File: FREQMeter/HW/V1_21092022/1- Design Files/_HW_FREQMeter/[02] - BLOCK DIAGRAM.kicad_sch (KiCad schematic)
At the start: 0 parts

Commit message: WORKING ON FREQMeter Hardware
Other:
- note added: "100MHz to 1.1 GHz Ratio 1:16"
- note added: "1Hz to 1MHz Ratio 1:1"
- note added: "1MHz to 100MHz Ratio 1:1024"
- note added: "32 SMD LEDs Binary Counter"
- note added: "4 X SHIFT REGISTER"
- note added: "Data Lines"
- note added: "Page 3"
- note added: "Page 4"
- note added: "Page 5"
- note added: "Page 6"
- note added: "X2 Buffer CLOCK Enable Pin"
- note added: "X2 Data Lines"
- note removed: "100MHz to 1.1 GHz dividing by 16"
- note removed: "1MHz to 100MHz dividing by 1024"
- note removed: "DC (0Hz) to 1MHz Ratio 1:1"

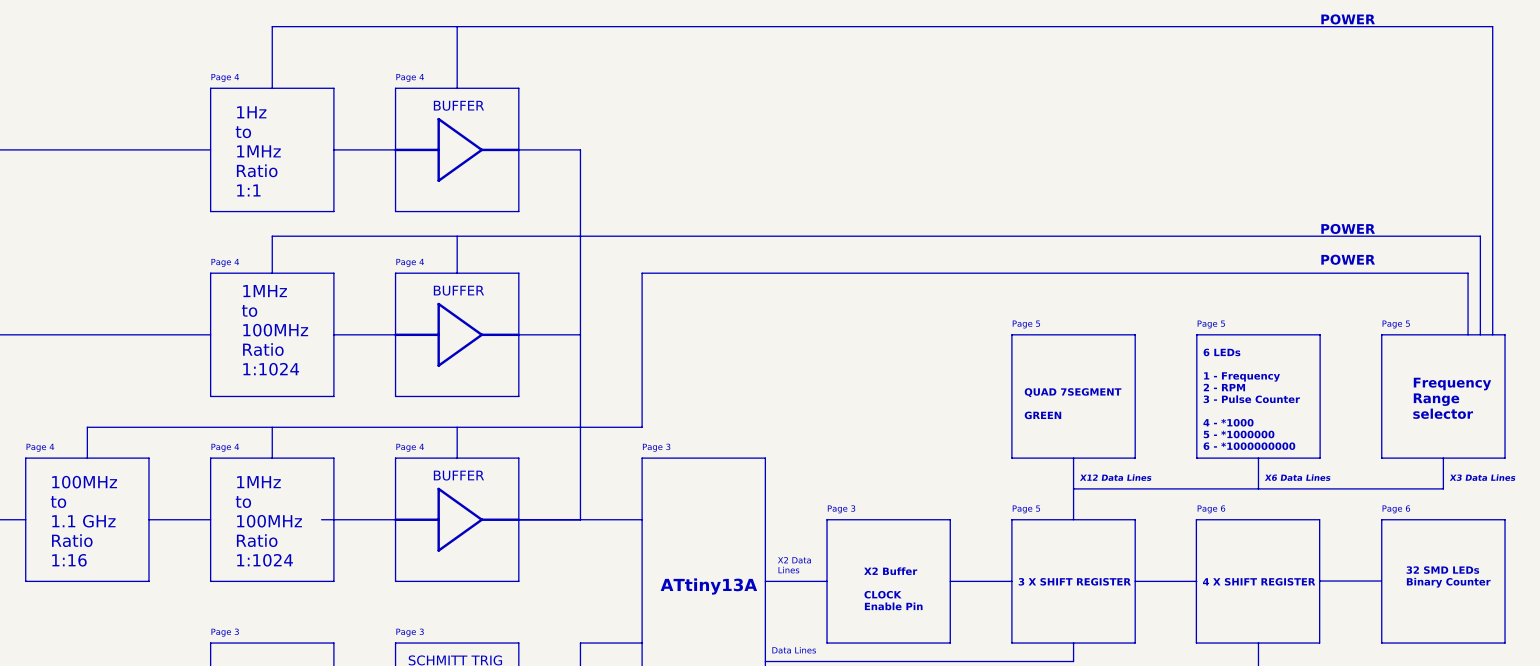
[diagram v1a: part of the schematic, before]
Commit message: progress on Frequency meter hardware
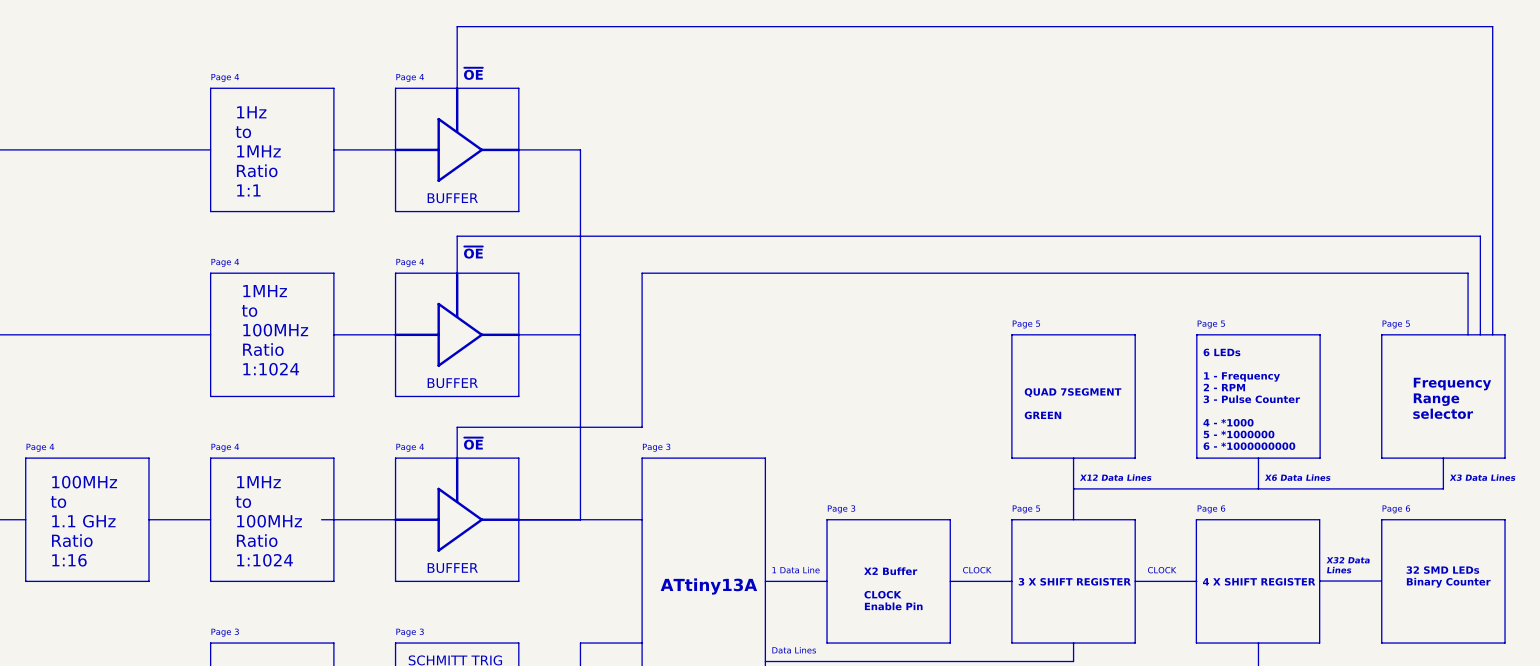
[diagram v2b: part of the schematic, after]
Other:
- note added: "1 Data Line"
- note added: "CLOCK"
- note added: "X32 Data Lines"
- note added: "~{OE}"
- note removed: "POWER"
- note removed: "X2 Data Lines"

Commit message: frequency meter input schematic in progress
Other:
- note added: "BNC Input & Matching Circuit"
- note added: "Filter BPF 1MHz To 99.999MHz"
- note added: "Filter LPF 1Hz To 999KHz"
- note added: "INPUT CIRCUIT"
- note added: "O1"
- note added: "O2"
- note added: "O3"
- note added: "OPEN-LOOP AMPLIFIRE"
- note added: "~{OE1}"
- note added: "~{OE2}"
- note added: "~{OE3}"
- note removed: "1Hz to 1MHz Ratio 1:1"
- note removed: "BNC Input"
- note removed: "Matching Circuit"
- note removed: "~{OE}"

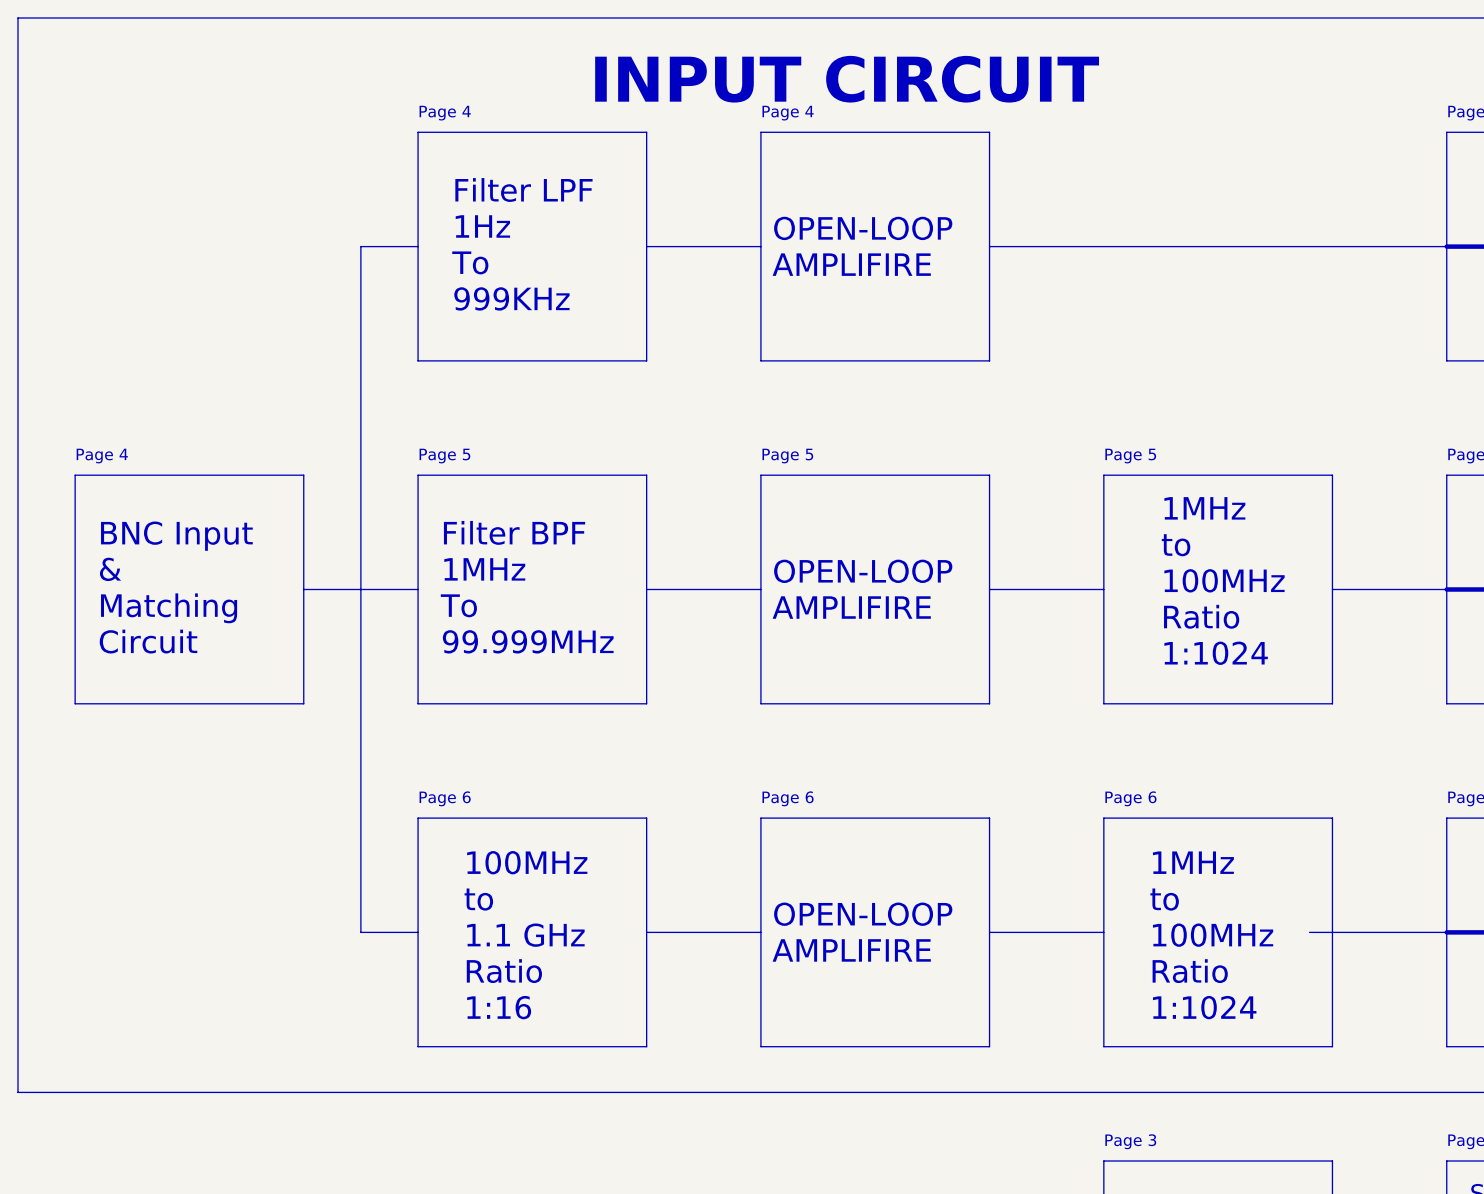
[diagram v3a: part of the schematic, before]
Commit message: Input signal schematic has been modified
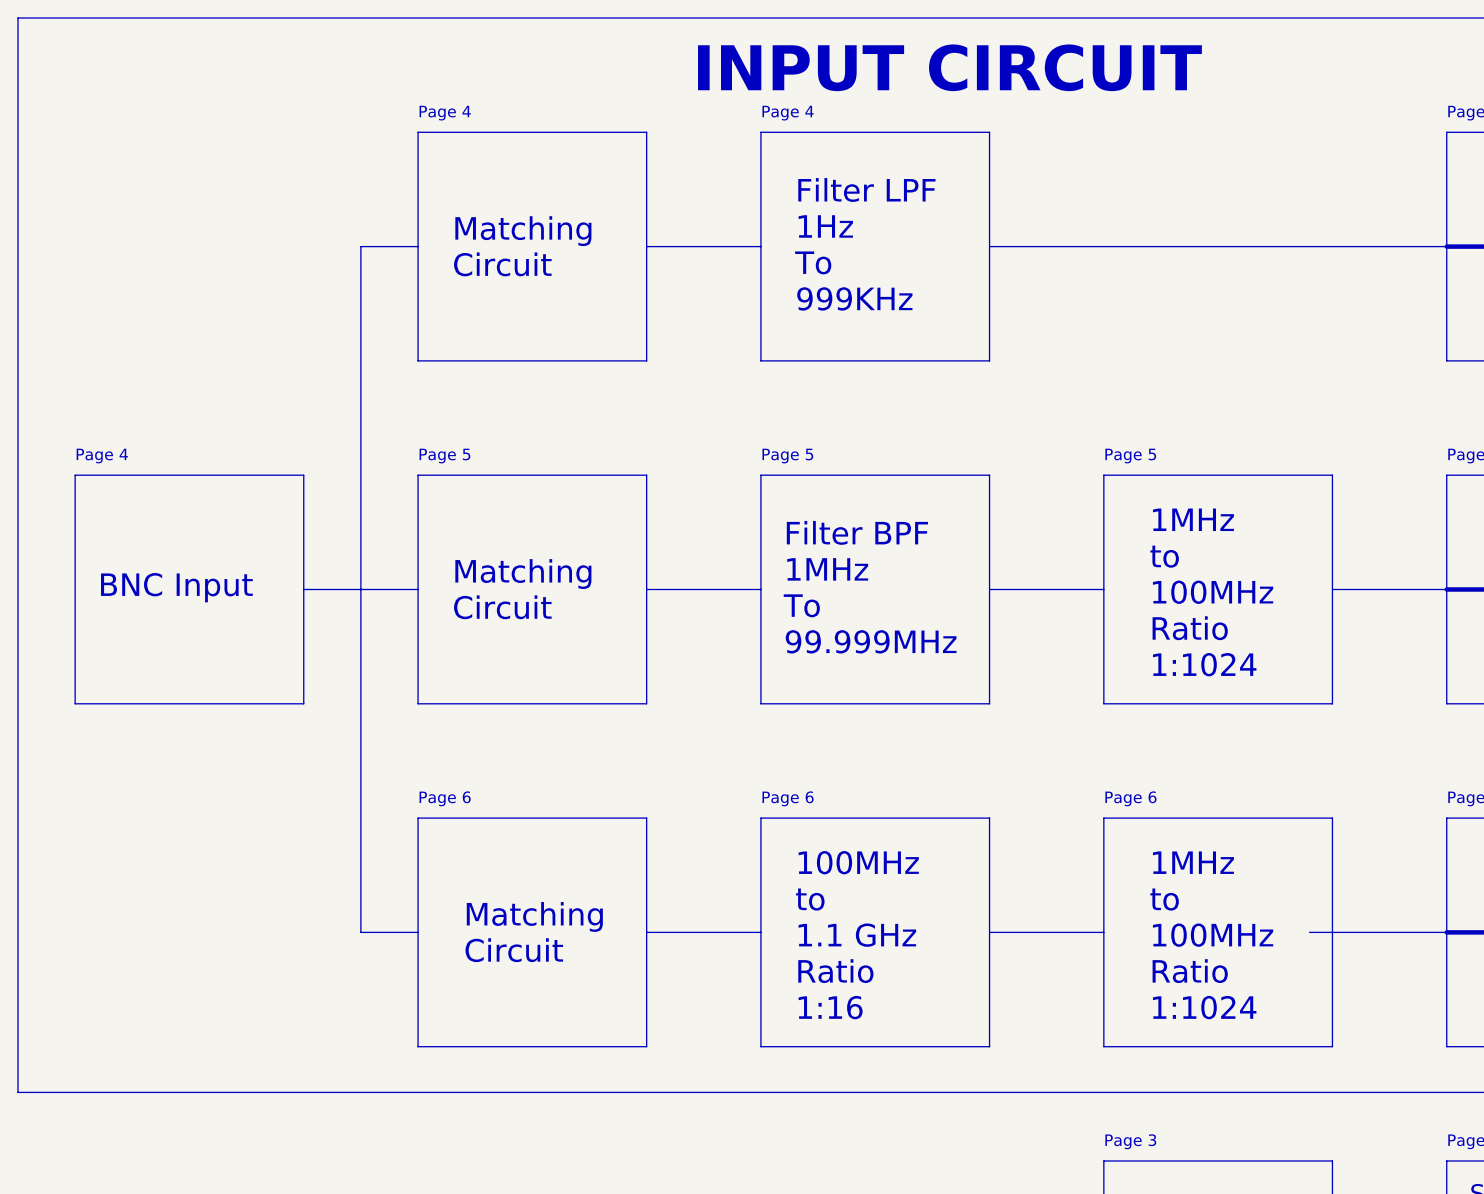
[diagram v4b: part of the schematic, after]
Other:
- note added: "BNC Input"
- note added: "Matching Circuit"
- note removed: "BNC Input & Matching Circuit"
- note removed: "OPEN-LOOP AMPLIFIRE"
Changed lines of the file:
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@@
     (effects (font (size 1.27 1.27)) (justify left bottom))
   )
-  (text "Filter LPF\n1Hz \nTo \n999KHz" (at 67.31 83.82 0)
+  (text "Filter LPF\n1Hz \nTo \n999KHz" (at 105.41 83.82 0)
     (effects (font (size 2.5 2.5)) (justify left bottom))
   )
@@
     (effects (font (size 1.27 1.27)) (justify left bottom))
   )
-  (text "OPEN-LOOP\nAMPLIFIRE" (at 102.87 80.01 0)
-    (effects (font (size 2.5 2.5)) (justify left bottom))
-  )
   (text "X32 Data\nLines" (at 369.57 163.83 0)
     (effects (font (size 1.27 1.27) (thickness 0.254) bold italic) (justify left bottom))
@@
     (effects (font (size 1.27 1.27)) (justify left bottom))
   )
-  (text "Filter BPF\n1MHz\nTo\n99.999MHz" (at 66.04 121.92 0)
+  (text "Filter BPF\n1MHz\nTo\n99.999MHz" (at 104.14 121.92 0)
     (effects (font (size 2.5 2.5)) (justify left bottom))
   )
@@
     (effects (font (size 1.5 1.5) (thickness 0.254) bold) (justify left bottom))
   )
+  (text "Matching \nCircuit" (at 67.31 80.01 0)
+    (effects (font (size 2.5 2.5)) (justify left bottom))
+  )
   (text "Page 5" (at 304.8 113.03 0)
     (effects (font (size 1.27 1.27)) (justify left bottom))
@@
     (effects (font (size 1.27 1.27)) (justify left bottom))
   )
+  (text "Matching \nCircuit" (at 68.58 156.21 0)
+    (effects (font (size 2.5 2.5)) (justify left bottom))
+  )
   (text "3 X SHIFT REGISTER" (at 306.07 166.37 0)
     (effects (font (size 1.5 1.5) (thickness 0.254) bold) (justify left bottom))
+  )
+  (text "Matching \nCircuit" (at 67.31 118.11 0)
+    (effects (font (size 2.5 2.5)) (justify left bottom))
   )
   (text "X6 Data Lines" (at 356.87 144.78 0)
@@
     (effects (font (size 1.5 1.5) (thickness 0.254) bold) (justify left bottom))
   )
-  (text "100MHz\nto\n1.1 GHz \nRatio\n1:16" (at 68.58 162.56 0)
+  (text "100MHz\nto\n1.1 GHz \nRatio\n1:16" (at 105.41 162.56 0)
     (effects (font (size 2.5 2.5)) (justify left bottom))
   )
@@
     (effects (font (size 1.27 1.27) (thickness 0.254) bold italic) (justify left bottom))
   )
-  (text "BNC Input\n&\nMatching \nCircuit" (at 27.94 121.92 0)
+  (text "BNC Input" (at 27.94 115.57 0)
     (effects (font (size 2.5 2.5)) (justify left bottom))
   )
@@
     (effects (font (size 1.27 1.27)) (justify left bottom))
   )
-  (text "1MHz\nto\n100MHz\nRatio\n1:1024" (at 146.05 123.19 0)
+  (text "1MHz\nto\n100MHz\nRatio\n1:1024" (at 144.78 124.46 0)
     (effects (font (size 2.5 2.5)) (justify left bottom))
   )
@@
     (effects (font (size 1.27 1.27)) (justify left bottom))
   )
-  (text "INPUT CIRCUIT" (at 82.55 60.96 0)
+  (text "INPUT CIRCUIT" (at 93.98 59.69 0)
     (effects (font (size 5 5) (thickness 1) bold) (justify left bottom))
   )
@@
     (effects (font (size 1.27 1.27)) (justify left bottom))
   )
-  (text "OPEN-LOOP\nAMPLIFIRE" (at 102.87 156.21 0)
-    (effects (font (size 2.5 2.5)) (justify left bottom))
-  )
   (text "Page 6" (at 381 151.13 0)
     (effects (font (size 1.27 1.27)) (justify left bottom))
@@
     (effects (font (size 1.27 1.27)) (justify left bottom))
   )
-  (text "OPEN-LOOP\nAMPLIFIRE" (at 102.87 118.11 0)
-    (effects (font (size 2.5 2.5)) (justify left bottom))
-  )
 )
